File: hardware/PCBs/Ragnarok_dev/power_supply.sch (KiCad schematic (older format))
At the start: 25 parts, among them Q1 Q_PMOS_GDS, Q2 Q_PMOS_GDS

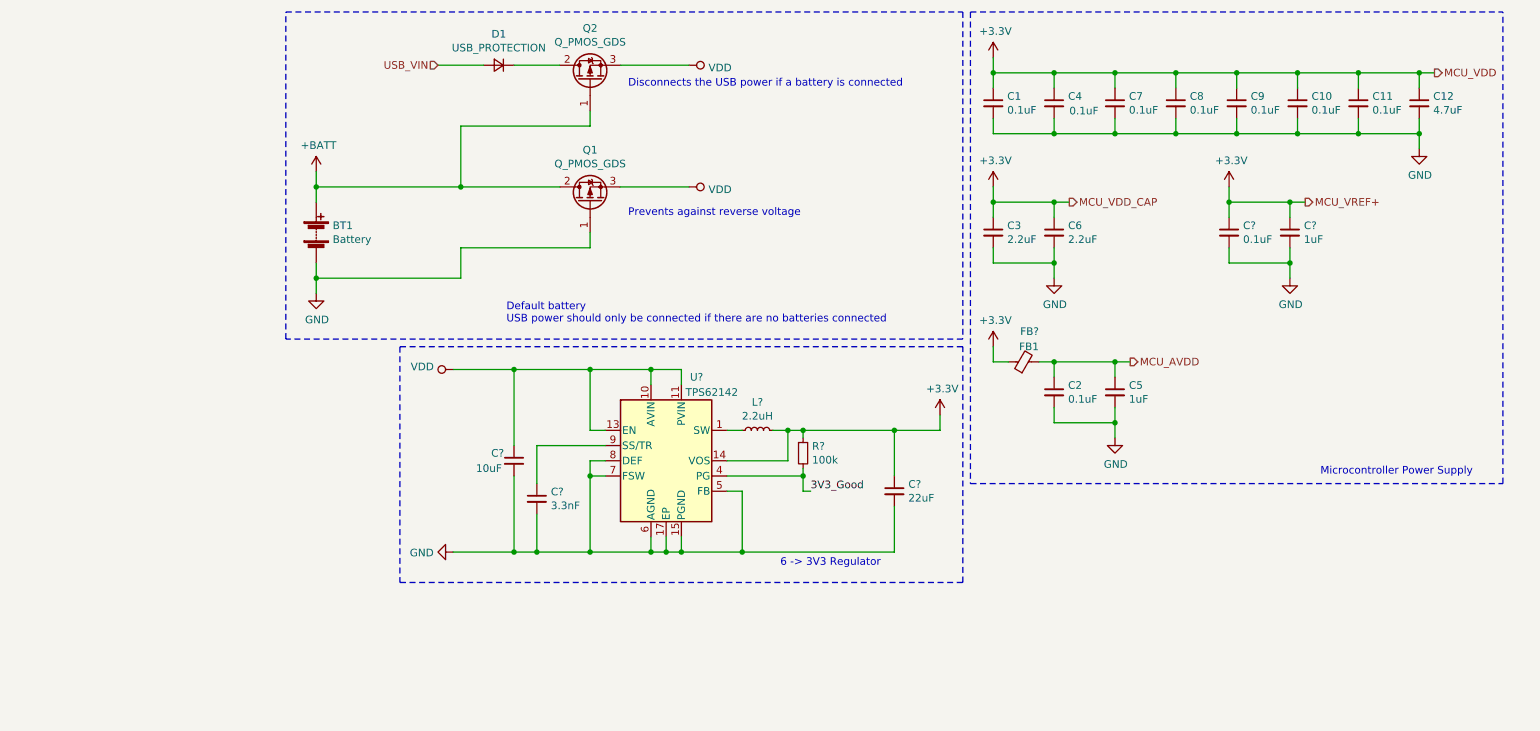
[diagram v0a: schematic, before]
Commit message: add spi sheet
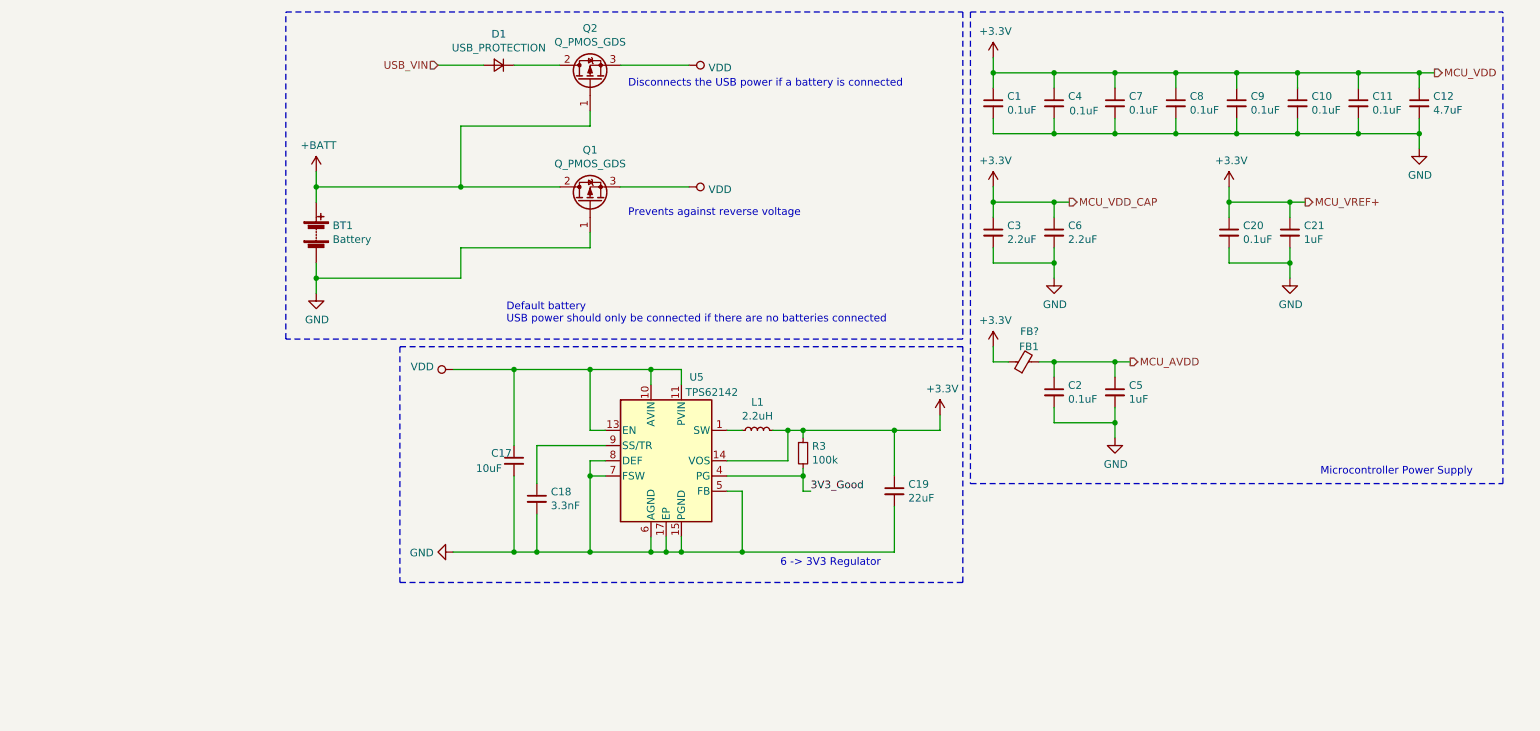
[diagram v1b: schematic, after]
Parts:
- gave numbers to parts that had none: 8
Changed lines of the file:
@@
 $Descr A4 11693 8268
 encoding utf-8
-Sheet 2 2
+Sheet 2 3
 Title "Ragnarok Development Board"
 Date "2019-12-18"
 Rev "v0.1"
 Comp "UAH Space Hardware Club"
-Comment1 "Shelby Tull"
+Comment1 ""
 Comment2 "Brennan Haralson"
 Comment3 "Shelby Westrich"
@@
 	5500 3100 5700 3100
 $Comp
-L power:VDD #PWR?
+L power:VDD #PWR0108
 U 1 1 5E0DFAB4
 P 4200 3100
-F 0 "#PWR?" H 4200 2950 50  0001 C CNN
+F 0 "#PWR0108" H 4200 2950 50  0001 C CNN
 F 1 "VDD" V 4218 3227 50  0000 L CNN
 F 2 "" H 4200 3100 50  0001 C CNN
@@
 $EndComp
 $Comp
-L power:GND #PWR?
+L power:GND #PWR0109
 U 1 1 5E0E056B
 P 4200 4300
-F 0 "#PWR?" H 4200 4050 50  0001 C CNN
+F 0 "#PWR0109" H 4200 4050 50  0001 C CNN
 F 1 "GND" V 4205 4172 50  0000 R CNN
 F 2 "" H 4200 4300 50  0001 C CNN
@@
 P 4600 3700
 AR Path="/5E0E46D2" Ref="C?"  Part="1"
-AR Path="/5DFDE168/5E0E46D2" Ref="C?"  Part="1"
-F 0 "C?" H 4450 3750 50  0000 L CNN
+AR Path="/5DFDE168/5E0E46D2" Ref="C17"  Part="1"
+F 0 "C17" H 4450 3750 50  0000 L CNN
 F 1 "10uF" H 4350 3650 50  0000 L CNN
 F 2 "Capacitor_SMD:C_0603_1608Metric_Pad1.05x0.95mm_HandSolder" H 4600 3700 50  0001 C CNN
@@
 P 4750 3950
 AR Path="/5E0E69DF" Ref="C?"  Part="1"
-AR Path="/5DFDE168/5E0E69DF" Ref="C?"  Part="1"
-F 0 "C?" H 4842 3996 50  0000 L CNN
+AR Path="/5DFDE168/5E0E69DF" Ref="C18"  Part="1"
+F 0 "C18" H 4842 3996 50  0000 L CNN
 F 1 "3.3nF" H 4842 3905 50  0000 L CNN
 F 2 "Capacitor_SMD:C_0603_1608Metric_Pad1.05x0.95mm_HandSolder" H 4750 3950 50  0001 C CNN
@@
 	4200 4300 4600 4300
 $Comp
-L Device:L_Small L?
+L Device:L_Small L1
 U 1 1 5E100CAE
 P 6200 3500
-F 0 "L?" V 6385 3500 50  0000 C CNN
+F 0 "L1" V 6385 3500 50  0000 C CNN
 F 1 "2.2uH" V 6294 3500 50  0000 C CNN
 F 2 "" H 6200 3500 50  0001 C CNN
@@
 	6400 3700 6400 3500
 $Comp
-L Regulator_Switching:TPS62142 U?
+L Regulator_Switching:TPS62142 U5
 U 1 1 5E0D9FD0
 P 5600 3700
-F 0 "U?" H 5800 4250 50  0000 C CNN
+F 0 "U5" H 5800 4250 50  0000 C CNN
 F 1 "TPS62142" H 5900 4150 50  0000 C CNN
 F 2 "Package_DFN_QFN:QFN-16-1EP_3x3mm_P0.5mm_EP1.8x1.8mm" H 5750 3250 50  0001 L CNN
@@
 	5100 3800 5100 4300
 $Comp
-L Device:R_Small R?
+L Device:R_Small R3
 U 1 1 5E112C69
 P 6500 3650
-F 0 "R?" H 6559 3696 50  0000 L CNN
+F 0 "R3" H 6559 3696 50  0000 L CNN
 F 1 "100k" H 6559 3605 50  0000 L CNN
 F 2 "" H 6500 3650 50  0001 C CNN
@@
 P 7100 3900
 AR Path="/5E130815" Ref="C?"  Part="1"
-AR Path="/5DFDE168/5E130815" Ref="C?"  Part="1"
-F 0 "C?" H 7192 3946 50  0000 L CNN
+AR Path="/5DFDE168/5E130815" Ref="C19"  Part="1"
+F 0 "C19" H 7192 3946 50  0000 L CNN
 F 1 "22uF" H 7192 3855 50  0000 L CNN
 F 2 "Capacitor_SMD:C_0603_1608Metric_Pad1.05x0.95mm_HandSolder" H 7100 3900 50  0001 C CNN
@@
 	5200 3600 4750 3600
 $Comp
-L power:+3.3V #PWR?
+L power:+3.3V #PWR0110
 U 1 1 5E150137
 P 7400 3400
-F 0 "#PWR?" H 7400 3250 50  0001 C CNN
+F 0 "#PWR0110" H 7400 3250 50  0001 C CNN
 F 1 "+3.3V" H 7415 3573 50  0000 C CNN
 F 2 "" H 7400 3400 50  0001 C CNN
@@
 	7550 2950 3850 2950
 $Comp
-L power:GND #PWR?
+L power:GND #PWR0111
 U 1 1 5E1B4404
 P 9700 2500
-F 0 "#PWR?" H 9700 2250 50  0001 C CNN
+F 0 "#PWR0111" H 9700 2250 50  0001 C CNN
 F 1 "GND" H 9705 2327 50  0000 C CNN
 F 2 "" H 9700 2500 50  0001 C CNN
@@
 	9300 1900 9300 2000
 $Comp
-L power:+3.3V #PWR?
+L power:+3.3V #PWR0112
 U 1 1 5E1B4414
 P 9300 1900
-F 0 "#PWR?" H 9300 1750 50  0001 C CNN
+F 0 "#PWR0112" H 9300 1750 50  0001 C CNN
 F 1 "+3.3V" H 9315 2073 50  0000 C CNN
 F 2 "" H 9300 1900 50  0001 C CNN
@@
 P 9700 2200
 AR Path="/5E1B441A" Ref="C?"  Part="1"
-AR Path="/5DFDE168/5E1B441A" Ref="C?"  Part="1"
-F 0 "C?" H 9792 2246 50  0000 L CNN
+AR Path="/5DFDE168/5E1B441A" Ref="C21"  Part="1"
+F 0 "C21" H 9792 2246 50  0000 L CNN
 F 1 "1uF" H 9792 2155 50  0000 L CNN
 F 2 "Capacitor_SMD:C_0603_1608Metric_Pad1.05x0.95mm_HandSolder" H 9700 2200 50  0001 C CNN
@@
 P 9300 2200
 AR Path="/5E1B4420" Ref="C?"  Part="1"
-AR Path="/5DFDE168/5E1B4420" Ref="C?"  Part="1"
-F 0 "C?" H 9392 2246 50  0000 L CNN
+AR Path="/5DFDE168/5E1B4420" Ref="C20"  Part="1"
+F 0 "C20" H 9392 2246 50  0000 L CNN
 F 1 "0.1uF" H 9392 2155 50  0000 L CNN
 F 2 "Capacitor_SMD:C_0603_1608Metric_Pad1.05x0.95mm_HandSolder" H 9300 2200 50  0001 C CNN

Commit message: Update
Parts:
- added C24: 1uF, symbol Device:C_Small
- added C25: 10nF, symbol Device:C_Small
- added C26: 2.2uF, symbol Device:C_Small
- added SW?: Power, symbol Switch:SW_SPDT
- added U6: LP2985-50DBVR, SOT23-5, symbol LP2985-50DBVR:LP2985-50DBVR
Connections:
- net labels added: +5V
- wire segments 124 -> 139
- no-connect marks 0 -> 1
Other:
- note added: "6 -> 5V Regulator\n"
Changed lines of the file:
@@
 $Descr A4 11693 8268
 encoding utf-8
-Sheet 2 3
+Sheet 2 4
 Title "Ragnarok Development Board"
 Date "2019-12-18"
@@
 L power:VDD #PWR08
 U 1 1 5E080DA6
-P 5750 1100
-F 0 "#PWR08" H 5750 950 50  0001 C CNN
-F 1 "VDD" V 5767 1228 50  0000 L CNN
-F 2 "" H 5750 1100 50  0001 C CNN
-F 3 "" H 5750 1100 50  0001 C CNN
-	1    5750 1100
-	0    1    1    0
-$EndComp
-$Comp
-L power:VDD #PWR07
-U 1 1 5E0819D7
-P 5750 1900
-F 0 "#PWR07" H 5750 1750 50  0001 C CNN
-F 1 "VDD" V 5767 2028 50  0000 L CNN
-F 2 "" H 5750 1900 50  0001 C CNN
-F 3 "" H 5750 1900 50  0001 C CNN
-	1    5750 1900
+P 6500 1650
+F 0 "#PWR08" H 6500 1500 50  0001 C CNN
+F 1 "VDD" V 6517 1778 50  0000 L CNN
+F 2 "" H 6500 1650 50  0001 C CNN
+F 3 "" H 6500 1650 50  0001 C CNN
+	1    6500 1650
 	0    1    1    0
 $EndComp
@@
 Text Notes 5350 2100 0    50   ~ 0
 Prevents against reverse voltage
-Text Notes 5350 1250 0    50   ~ 0
+Text Notes 5450 1000 0    50   ~ 0
 Disconnects the USB power if a battery is connected
 Wire Wire Line
@@
 	6500 3500 7100 3500
 Connection ~ 6500 3500
-Connection ~ 7100 3500
-Wire Wire Line
-	7100 3500 7400 3500
 Wire Wire Line
 	7100 4300 6100 4300
@@
 L power:+3.3V #PWR0110
 U 1 1 5E150137
-P 7400 3400
-F 0 "#PWR0110" H 7400 3250 50  0001 C CNN
-F 1 "+3.3V" H 7415 3573 50  0000 C CNN
-F 2 "" H 7400 3400 50  0001 C CNN
-F 3 "" H 7400 3400 50  0001 C CNN
-	1    7400 3400
-	1    0    0    -1
-$EndComp
-Wire Wire Line
-	7400 3500 7400 3400
+P 7200 3500
+F 0 "#PWR0110" H 7200 3350 50  0001 C CNN
+F 1 "+3.3V" V 7300 3550 50  0000 C CNN
+F 2 "" H 7200 3500 50  0001 C CNN
+F 3 "" H 7200 3500 50  0001 C CNN
+	1    7200 3500
+	0    1    1    0
+$EndComp
 Wire Wire Line
 	5600 4200 5600 4300
@@
 	8550 3050 8650 3050
 Connection ~ 8550 3050
+$Comp
+L LP2985-50DBVR:LP2985-50DBVR U6
+U 1 1 5E21B885
+P 9400 4650
+F 0 "U6" H 9400 5317 50  0000 C CNN
+F 1 "LP2985-50DBVR" H 9400 5226 50  0000 C CNN
+F 2 "SOT23-5" H 9400 4650 50  0001 L BNN
+F 3 "" H 9400 4650 50  0001 C CNN
+	1    9400 4650
+	1    0    0    -1
+$EndComp
+$Comp
+L power:VDD #PWR0114
+U 1 1 5E21CD3F
+P 7900 4450
+F 0 "#PWR0114" H 7900 4300 50  0001 C CNN
+F 1 "VDD" V 7918 4577 50  0000 L CNN
+F 2 "" H 7900 4450 50  0001 C CNN
+F 3 "" H 7900 4450 50  0001 C CNN
+	1    7900 4450
+	0    -1   -1   0
+$EndComp
+$Comp
+L Device:C_Small C24
+U 1 1 5E21D741
+P 8450 4550
+F 0 "C24" H 8358 4504 50  0000 R CNN
+F 1 "1uF" H 8358 4595 50  0000 R CNN
+F 2 "" H 8450 4550 50  0001 C CNN
+F 3 "~" H 8450 4550 50  0001 C CNN
+	1    8450 4550
+	1    0    0    1
+$EndComp
+Wire Wire Line
+	7900 4450 8150 4450
+Connection ~ 8450 4450
+Wire Wire Line
+	8800 4650 8450 4650
+Wire Wire Line
+	8450 4450 8800 4450
+$Comp
+L Device:C_Small C26
+U 1 1 5E2361E6
+P 10600 4650
+F 0 "C26" H 10508 4604 50  0000 R CNN
+F 1 "2.2uF" H 10508 4695 50  0000 R CNN
+F 2 "" H 10600 4650 50  0001 C CNN
+F 3 "~" H 10600 4650 50  0001 C CNN
+	1    10600 4650
+	-1   0    0    1
+$EndComp
+$Comp
+L Device:C_Small C25
+U 1 1 5E236D16
+P 10200 4850
+F 0 "C25" V 9971 4850 50  0000 C CNN
+F 1 "10nF" V 10062 4850 50  0000 C CNN
+F 2 "" H 10200 4850 50  0001 C CNN
+F 3 "~" H 10200 4850 50  0001 C CNN
+	1    10200 4850
+	0    -1   1    0
+$EndComp
+Wire Wire Line
+	8800 4850 8150 4850
+Wire Wire Line
+	8150 4850 8150 4450
+Connection ~ 8150 4450
+Wire Wire Line
+	8150 4450 8450 4450
+Wire Wire Line
+	10000 4450 10600 4450
+$Comp
+L power:GND #PWR0115
+U 1 1 5E24E875
+P 10600 4950
+F 0 "#PWR0115" H 10600 4700 50  0001 C CNN
+F 1 "GND" H 10605 4777 50  0000 C CNN
+F 2 "" H 10600 4950 50  0001 C CNN
+F 3 "" H 10600 4950 50  0001 C CNN
+	1    10600 4950
+	1    0    0    -1
+$EndComp
+Wire Wire Line
+	10000 4850 10100 4850
+Wire Wire Line
+	10600 4450 10600 4550
+Wire Wire Line
+	10300 4850 10600 4850
+Wire Wire Line
+	10600 4850 10600 4750
+Wire Wire Line
+	10600 4850 10600 4950
+Connection ~ 10600 4850
+Text Notes 10150 5350 0    50   ~ 0
+6 -> 5V Regulator\n
+Wire Notes Line
+	7600 3900 7600 5400
+$Comp
+L power:+5V #PWR0116
+U 1 1 5E2A1659
+P 10700 4450
+F 0 "#PWR0116" H 10700 4300 50  0001 C CNN
+F 1 "+5V" V 10715 4578 50  0000 L CNN
+F 2 "" H 10700 4450 50  0001 C CNN
+F 3 "" H 10700 4450 50  0001 C CNN
+	1    10700 4450
+	0    1    1    0
+$EndComp
+Wire Wire Line
+	7100 3500 7200 3500
+Connection ~ 7100 3500
+Wire Wire Line
+	10600 4450 10700 4450
+Connection ~ 10600 4450
+Wire Notes Line
+	7600 3900 11050 3900
+Wire Notes Line
+	7600 5400 11050 5400
+Wire Notes Line
+	11050 3900 11050 5400
+$Comp
+L Switch:SW_SPDT SW?
+U 1 1 5E2C29FA
+P 6300 1550
+AR Path="/5E2C29FA" Ref="SW?"  Part="1"
+AR Path="/5DFDE168/5E2C29FA" Ref="SW?"  Part="1"
+F 0 "SW?" H 6150 1350 50  0000 C CNN
+F 1 "Power" H 6100 1450 50  0000 C CNN
+F 2 "" H 6300 1550 50  0001 C CNN
+F 3 "" H 6300 1550 50  0001 C CNN
+	1    6300 1550
+	1    0    0    1
+$EndComp
+Wire Wire Line
+	5750 1100 5750 1550
+Wire Wire Line
+	5750 1550 6100 1550
+Wire Wire Line
+	5750 1900 5750 1550
+Connection ~ 5750 1550
+NoConn ~ 6500 1450
 $EndSCHEMATC

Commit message: UART
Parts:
- U6: footprint SOT23-5 -> LP2985:SOT23-5
- gave numbers to parts that had none: 1
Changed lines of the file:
@@
 $Descr A4 11693 8268
 encoding utf-8
-Sheet 2 4
+Sheet 2 5
 Title "Ragnarok Development Board"
 Date "2019-12-18"
@@
 F 0 "U6" H 9400 5317 50  0000 C CNN
 F 1 "LP2985-50DBVR" H 9400 5226 50  0000 C CNN
-F 2 "SOT23-5" H 9400 4650 50  0001 L BNN
+F 2 "LP2985:SOT23-5" H 9400 4650 50  0001 L BNN
 F 3 "" H 9400 4650 50  0001 C CNN
 	1    9400 4650
@@
 P 6300 1550
 AR Path="/5E2C29FA" Ref="SW?"  Part="1"
-AR Path="/5DFDE168/5E2C29FA" Ref="SW?"  Part="1"
-F 0 "SW?" H 6150 1350 50  0000 C CNN
+AR Path="/5DFDE168/5E2C29FA" Ref="SW3"  Part="1"
+F 0 "SW3" H 6150 1350 50  0000 C CNN
 F 1 "Power" H 6100 1450 50  0000 C CNN
 F 2 "" H 6300 1550 50  0001 C CNN

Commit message: work
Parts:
- removed C26: 2.2uF, symbol Device:C_Small
- removed U6: LP2985-50DBVR, LP2985:SOT23-5, symbol LP2985-50DBVR:LP2985-50DBVR
- added U6: RT9069-50GB, symbol CUSTOM_COMPONENTS:RT9069-50GB
- C25: value 10nF -> 1uF
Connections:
- wire segments 139 -> 140
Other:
- moved on the sheet: C24
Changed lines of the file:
@@
 Connection ~ 8550 3050
-$Comp
-L LP2985-50DBVR:LP2985-50DBVR U6
-U 1 1 5E21B885
-P 9400 4650
-F 0 "U6" H 9400 5317 50  0000 C CNN
-F 1 "LP2985-50DBVR" H 9400 5226 50  0000 C CNN
-F 2 "LP2985:SOT23-5" H 9400 4650 50  0001 L BNN
-F 3 "" H 9400 4650 50  0001 C CNN
-	1    9400 4650
-	1    0    0    -1
-$EndComp
 $Comp
 L power:VDD #PWR0114
@@
 L Device:C_Small C24
 U 1 1 5E21D741
-P 8450 4550
-F 0 "C24" H 8358 4504 50  0000 R CNN
-F 1 "1uF" H 8358 4595 50  0000 R CNN
-F 2 "" H 8450 4550 50  0001 C CNN
-F 3 "~" H 8450 4550 50  0001 C CNN
-	1    8450 4550
+P 8700 4800
+F 0 "C24" H 8608 4754 50  0000 R CNN
+F 1 "1uF" H 8608 4845 50  0000 R CNN
+F 2 "" H 8700 4800 50  0001 C CNN
+F 3 "~" H 8700 4800 50  0001 C CNN
+	1    8700 4800
 	1    0    0    1
 $EndComp
-Wire Wire Line
-	7900 4450 8150 4450
-Connection ~ 8450 4450
-Wire Wire Line
-	8800 4650 8450 4650
-Wire Wire Line
-	8450 4450 8800 4450
-$Comp
-L Device:C_Small C26
-U 1 1 5E2361E6
-P 10600 4650
-F 0 "C26" H 10508 4604 50  0000 R CNN
-F 1 "2.2uF" H 10508 4695 50  0000 R CNN
-F 2 "" H 10600 4650 50  0001 C CNN
-F 3 "~" H 10600 4650 50  0001 C CNN
-	1    10600 4650
-	-1   0    0    1
-$EndComp
-$Comp
-L Device:C_Small C25
-U 1 1 5E236D16
-P 10200 4850
-F 0 "C25" V 9971 4850 50  0000 C CNN
-F 1 "10nF" V 10062 4850 50  0000 C CNN
-F 2 "" H 10200 4850 50  0001 C CNN
-F 3 "~" H 10200 4850 50  0001 C CNN
-	1    10200 4850
-	0    -1   1    0
-$EndComp
-Wire Wire Line
-	8800 4850 8150 4850
-Wire Wire Line
-	8150 4850 8150 4450
-Connection ~ 8150 4450
-Wire Wire Line
-	8150 4450 8450 4450
-Wire Wire Line
-	10000 4450 10600 4450
 $Comp
 L power:GND #PWR0115
 U 1 1 5E24E875
-P 10600 4950
-F 0 "#PWR0115" H 10600 4700 50  0001 C CNN
-F 1 "GND" H 10605 4777 50  0000 C CNN
-F 2 "" H 10600 4950 50  0001 C CNN
-F 3 "" H 10600 4950 50  0001 C CNN
-	1    10600 4950
+P 9350 5150
+F 0 "#PWR0115" H 9350 4900 50  0001 C CNN
+F 1 "GND" H 9355 4977 50  0000 C CNN
+F 2 "" H 9350 5150 50  0001 C CNN
+F 3 "" H 9350 5150 50  0001 C CNN
+	1    9350 5150
 	1    0    0    -1
 $EndComp
-Wire Wire Line
-	10000 4850 10100 4850
-Wire Wire Line
-	10600 4450 10600 4550
-Wire Wire Line
-	10300 4850 10600 4850
-Wire Wire Line
-	10600 4850 10600 4750
-Wire Wire Line
-	10600 4850 10600 4950
-Connection ~ 10600 4850
 Text Notes 10150 5350 0    50   ~ 0
 6 -> 5V Regulator\n
 Wire Notes Line
 	7600 3900 7600 5400
-$Comp
-L power:+5V #PWR0116
-U 1 1 5E2A1659
-P 10700 4450
-F 0 "#PWR0116" H 10700 4300 50  0001 C CNN
-F 1 "+5V" V 10715 4578 50  0000 L CNN
-F 2 "" H 10700 4450 50  0001 C CNN
-F 3 "" H 10700 4450 50  0001 C CNN
-	1    10700 4450
-	0    1    1    0
-$EndComp
 Wire Wire Line
 	7100 3500 7200 3500
 Connection ~ 7100 3500
-Wire Wire Line
-	10600 4450 10700 4450
-Connection ~ 10600 4450
 Wire Notes Line
 	7600 3900 11050 3900
@@
 Connection ~ 5750 1550
 NoConn ~ 6500 1450
+$Comp
+L CUSTOM_COMPONENTS:RT9069-50GB U6
+U 1 1 5E3227B1
+P 9350 4200
+F 0 "U6" H 9350 4215 50  0000 C CNN
+F 1 "RT9069-50GB" H 9350 4124 50  0000 C CNN
+F 2 "" H 9350 4200 50  0001 C CNN
+F 3 "" H 9350 4200 50  0001 C CNN
+	1    9350 4200
+	1    0    0    -1
+$EndComp
+Wire Wire Line
+	9350 5150 9350 5050
+$Comp
+L Device:C_Small C25
+U 1 1 5E33E835
+P 10000 4750
+F 0 "C25" H 9908 4704 50  0000 R CNN
+F 1 "1uF" H 9908 4795 50  0000 R CNN
+F 2 "" H 10000 4750 50  0001 C CNN
+F 3 "~" H 10000 4750 50  0001 C CNN
+	1    10000 4750
+	1    0    0    1
+$EndComp
+Wire Wire Line
+	9350 5050 10000 5050
+Wire Wire Line
+	10000 5050 10000 4850
+Connection ~ 9350 5050
+Wire Wire Line
+	9350 5050 9350 4950
+Wire Wire Line
+	9800 4450 10000 4450
+Wire Wire Line
+	10000 4450 10000 4650
+Wire Wire Line
+	10000 4450 10250 4450
+Connection ~ 10000 4450
+$Comp
+L power:+5V #PWR0116
+U 1 1 5E350D60
+P 10250 4450
+F 0 "#PWR0116" H 10250 4300 50  0001 C CNN
+F 1 "+5V" V 10265 4578 50  0000 L CNN
+F 2 "" H 10250 4450 50  0001 C CNN
+F 3 "" H 10250 4450 50  0001 C CNN
+	1    10250 4450
+	0    1    1    0
+$EndComp
+Wire Wire Line
+	7900 4450 8700 4450
+Wire Wire Line
+	8700 4450 8700 4600
+Wire Wire Line
+	8700 4600 8900 4600
+Connection ~ 8700 4450
+Wire Wire Line
+	8700 4450 8900 4450
+Connection ~ 8700 4600
+Wire Wire Line
+	8700 4600 8700 4700
+Wire Wire Line
+	8700 4900 8700 5050
+Wire Wire Line
+	8700 5050 9350 5050
 $EndSCHEMATC

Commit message: update
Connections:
- net VDD renamed +6V
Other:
- note added: "This needs to be fixed , currently floats\n"
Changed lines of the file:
@@
-$EndComp
-$Comp
-L power:+BATT #PWR02
-U 1 1 5E0636A5
-P 3300 1800
-F 0 "#PWR02" H 3300 1650 50  0001 C CNN
-F 1 "+BATT" H 3315 1973 50  0000 C CNN
-F 2 "" H 3300 1800 50  0001 C CNN
-F 3 "" H 3300 1800 50  0001 C CNN
-	1    3300 1800
-	1    0    0    -1
 $EndComp
 $Comp
@@
 Disconnects the USB power if a battery is connected
 Wire Wire Line
-	3300 1800 3300 1900
-Wire Wire Line
-	3300 1900 4250 1900
-Wire Wire Line
 	3300 2000 3300 1900
-Connection ~ 3300 1900
 $Comp
 L power:GND #PWR0101
@@
 Wire Wire Line
 	8700 5050 9350 5050
+$Comp
+L power:VDD #PWR?
+U 1 1 5E473C09
+P 6150 2500
+F 0 "#PWR?" H 6150 2350 50  0001 C CNN
+F 1 "VDD" V 6167 2628 50  0000 L CNN
+F 2 "" H 6150 2500 50  0001 C CNN
+F 3 "" H 6150 2500 50  0001 C CNN
+	1    6150 2500
+	0    -1   -1   0
+$EndComp
+$Comp
+L power:+6V #PWR?
+U 1 1 5E4741CD
+P 6400 2500
+F 0 "#PWR?" H 6400 2350 50  0001 C CNN
+F 1 "+6V" V 6415 2628 50  0000 L CNN
+F 2 "" H 6400 2500 50  0001 C CNN
+F 3 "" H 6400 2500 50  0001 C CNN
+	1    6400 2500
+	0    1    1    0
+$EndComp
+Wire Wire Line
+	6150 2500 6400 2500
+Text Notes 3400 1350 0    50   ~ 0
+This needs to be fixed , currently floats\n
+Wire Wire Line
+	3300 1900 4250 1900
+Wire Wire Line
+	3300 1800 3300 1900
+Connection ~ 3300 1900
+$Comp
+L power:+BATT #PWR02
+U 1 1 5E0636A5
+P 3300 1800
+F 0 "#PWR02" H 3300 1650 50  0001 C CNN
+F 1 "+BATT" H 3315 1973 50  0000 C CNN
+F 2 "" H 3300 1800 50  0001 C CNN
+F 3 "" H 3300 1800 50  0001 C CNN
+	1    3300 1800
+	1    0    0    -1
+$EndComp
 $EndSCHEMATC

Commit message: much schematic work
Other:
- note added: "Really need to look into the feasibility of this"
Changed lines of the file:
@@
 $Descr A4 11693 8268
 encoding utf-8
-Sheet 2 5
+Sheet 2 6
 Title "Ragnarok Development Board"
 Date "2019-12-18"
@@
 	1    0    0    -1
 $EndComp
+Text Notes 1300 900  0    50   ~ 0
+Really need to look into the feasibility of this
 $EndSCHEMATC
